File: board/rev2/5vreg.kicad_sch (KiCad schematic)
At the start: 20 parts

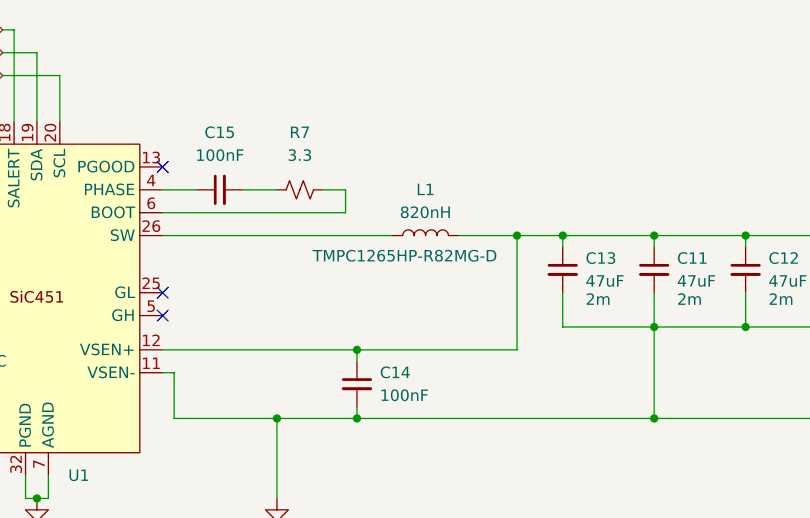
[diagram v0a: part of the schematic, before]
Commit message: Continue board work
- move to rp2040, separate stm32g071 to do usb-c + aux ctrl IO
  - still cheaper lol with the cost of stm32s
- more power reg stuff
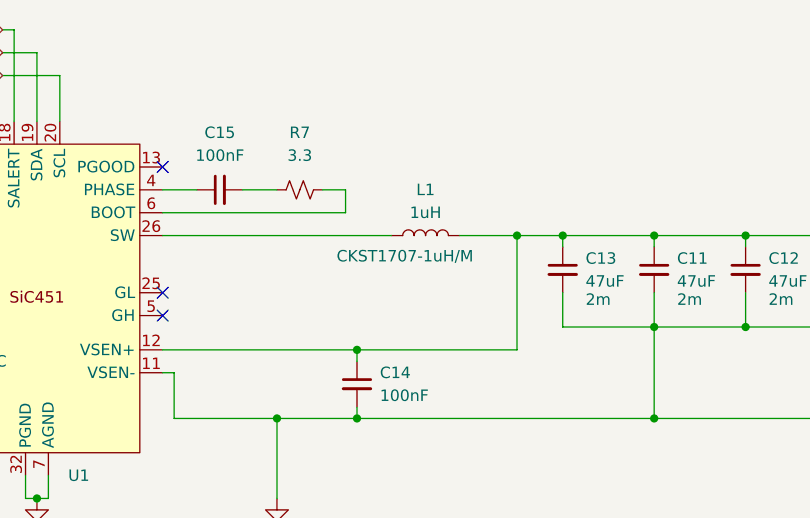
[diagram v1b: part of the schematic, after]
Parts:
- L1: value 820nH -> 1uH; Part TMPC1265HP-R82MG-D -> CKST1707-1uH/M
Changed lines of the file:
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@@
 			)
 		)
-		(property "Value" "820nH"
+		(property "Value" "1uH"
 			(at 198.12 85.09 90)
 			(effects
@@
 			)
 		)
-		(property "Part" "TMPC1265HP-R82MG-D"
+		(property "Part" "CKST1707-1uH/M"
 			(at 195.834 89.916 90)
 			(effects

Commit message: Board GPIO allocation
- and usbmux

still need to do termination on the big buses + a bunch of bypass caps
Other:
- company: (none) -> MLABS
- title: (none) -> USB PD 5V Regulator
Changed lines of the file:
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@@
 	(generator_version "9.0")
 	(paper "A4")
+	(title_block
+		(title "USB PD 5V Regulator")
+		(rev "A")
+		(company "MLABS")
+		(comment 1 "MSign-NG")
+	)
 	(junction
 		(at 68.58 80.01)

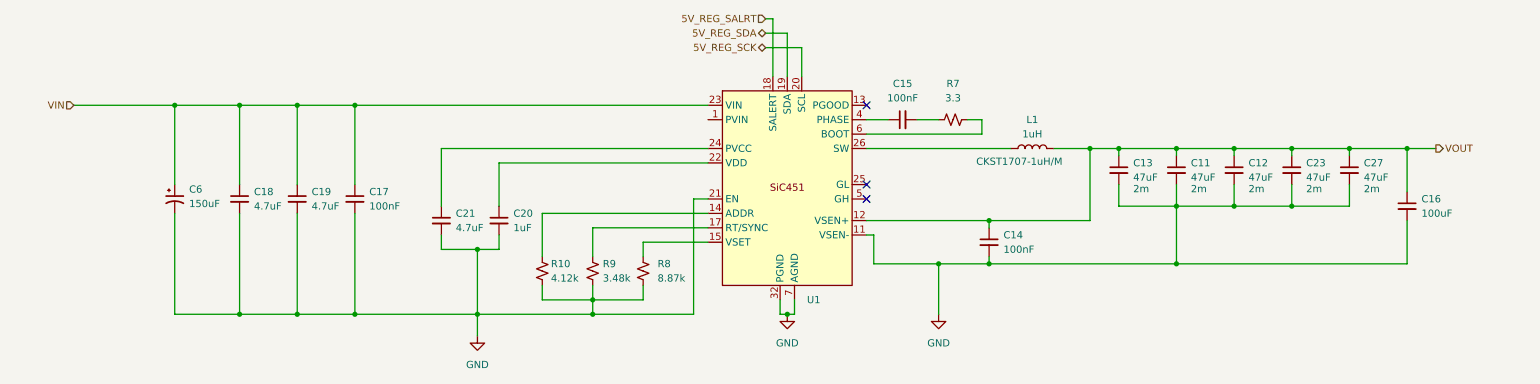
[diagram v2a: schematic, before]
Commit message: Continue board, assign caps/res, adjust for JLC availability
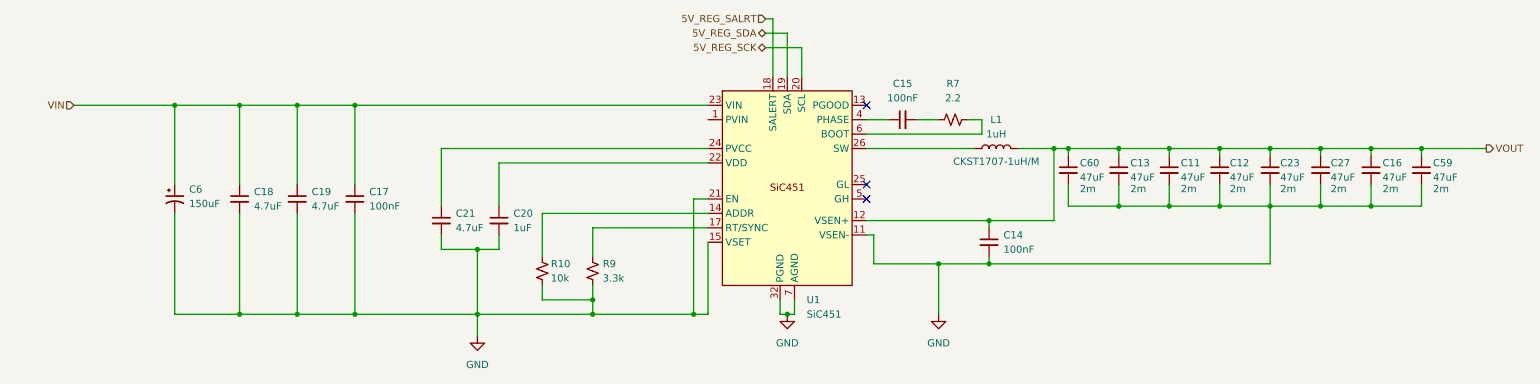
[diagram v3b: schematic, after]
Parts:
- removed R8: 8.87k, symbol Device:R_Small_US
- added C59, C60: 47uF, Capacitor_SMD:C_1206_3216Metric, symbol Device:C_Small
- C11, C12, C13, C23, C27: footprint (none) -> Capacitor_SMD:C_1206_3216Metric; Part (none) -> CL31A476MPHNNNE
- C14, C15, C17: footprint (none) -> Capacitor_SMD:C_0402_1005Metric; Part (none) -> CL05B104KB54PNC
- C16: value 100uF -> 47uF; footprint (none) -> Capacitor_SMD:C_1206_3216Metric; ESR (none) -> 2m; Part (none) -> CL31A476MPHNNNE
- C18, C19, C21: footprint (none) -> Capacitor_SMD:C_1206_3216Metric; Part (none) -> 1206B475K500NT
- C20: footprint (none) -> Capacitor_SMD:C_0603_1608Metric; Part (none) -> CL10A105KB8NNNC
- C6: footprint (none) -> Capacitor_THT:CP_Radial_D8.0mm_P3.50mm; Part (none) -> ERS1VM151F12OT
- L1: footprint (none) -> Inductor_Cenker:L_Cenker_CKST1707
- R10: value 4.12k -> 10k; footprint (none) -> Resistor_SMD:R_0805_2012Metric; Part (none) -> 0805W8F1002T5E
- R7: value 3.3 -> 2.2; footprint (none) -> Resistor_SMD:R_0603_1608Metric; Part (none) -> 0603WAF220KT5E
- R9: value 3.48k -> 3.3k; footprint (none) -> Resistor_SMD:R_0402_1005Metric; Part (none) -> 0402WGF3301TCE
- U1: value ~ -> SiC451
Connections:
- net GND: now also U1.15 (VSET), C59.2, C60.2
- net VOUT: now also C59.1, C60.1
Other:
- moved on the sheet: C11, C12, C23, C27, L1

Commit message: Start new PCB
- all footprints setup
- need to setup netclasses next, tho
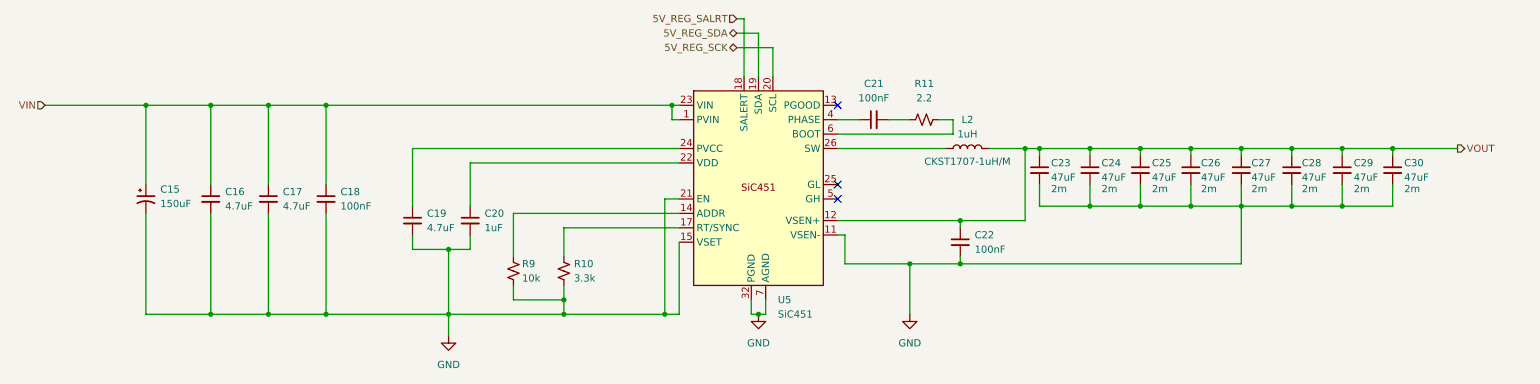
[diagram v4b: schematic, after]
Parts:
- U5: renamed from U1; Part (none) -> SiC451
- renumbered C6 to C15, C18 to C16, C19 to C17, C17 to C18, C21 to C19, C15 to C21, C14 to C22, C60 to C23, C13 to C24, C11 to C25, C12 to C26, C23 to C27, C27 to C28, C16 to C29, C59 to C30, L1 to L2, R9 to R10, R7 to R11, R10 to R9
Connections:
- net VIN: now also U5.1 (PVIN)
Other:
- moved on the sheet: C15, C16, C17, C18, C19, C20, C21, C22, C23, C24, C25, C26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

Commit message: Really finish rev2 board schematic
- fix some more footprints
  - move to real SD card holder, for example
- repair part numbers
- add LCSC part refs to everything
- add even more caps to the 3.3V reg output
  - really should use an LDO but meh it should be fine

total BOM cost for 5 of them is apparently 160 CAD, or like 32 dollars
each (don't think that includes the feeder fees tho)
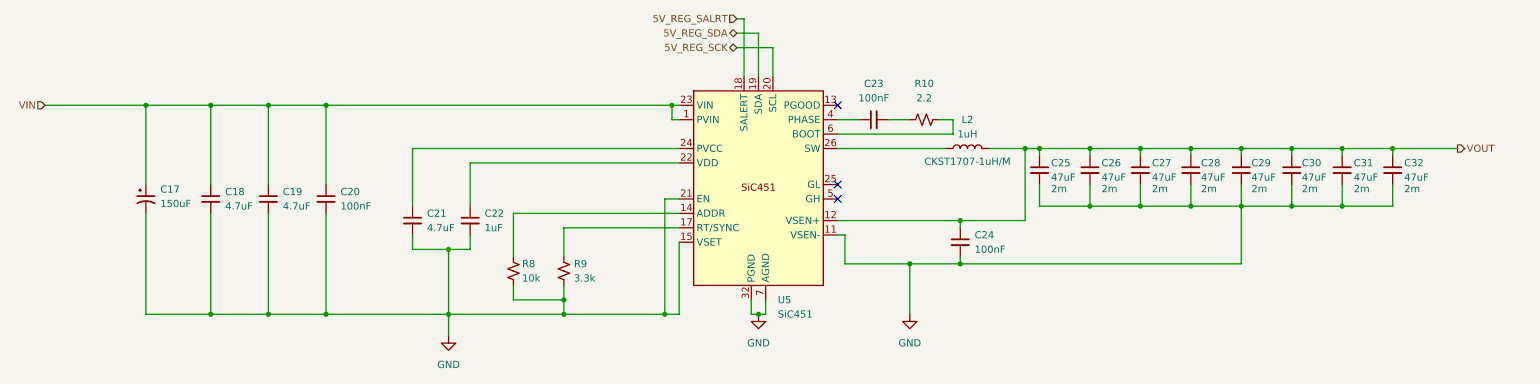
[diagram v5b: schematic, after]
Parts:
- C17: renamed from C15; LCSC (none) -> C106696
- C18: renamed from C16; LCSC (none) -> C29823
- C19: renamed from C17; LCSC (none) -> C29823
- C20: renamed from C18; LCSC (none) -> C307331
- C21: renamed from C19; LCSC (none) -> C29823
- C22: renamed from C20; LCSC (none) -> C15849
- C23: renamed from C21; LCSC (none) -> C307331
- C24: renamed from C22; LCSC (none) -> C307331
- C25: renamed from C23; LCSC (none) -> C96123
- C26: renamed from C24; LCSC (none) -> C96123
- C27: renamed from C25; LCSC (none) -> C96123
- C28: renamed from C26; LCSC (none) -> C96123
- C29: renamed from C27; LCSC (none) -> C96123
- C30: renamed from C28; LCSC (none) -> C96123
- C31: renamed from C29; LCSC (none) -> C96123
- C32: renamed from C30; LCSC (none) -> C96123
- L2: LCSC (none) -> C5292052
- R10: renamed from R11; LCSC (none) -> C22939
- R8: renamed from R9; LCSC (none) -> C17414
- R9: renamed from R10; LCSC (none) -> C25890
- U5: LCSC (none) -> C1852144; Part SiC451 -> SIC451ED-T1-GE3

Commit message: Start board
add a few extra bypass caps too, and swap some pins on the USB mux

i forgot to add a bypass cap on the tpd6s so that also needs to happen

truly 63 capacitors is not enough
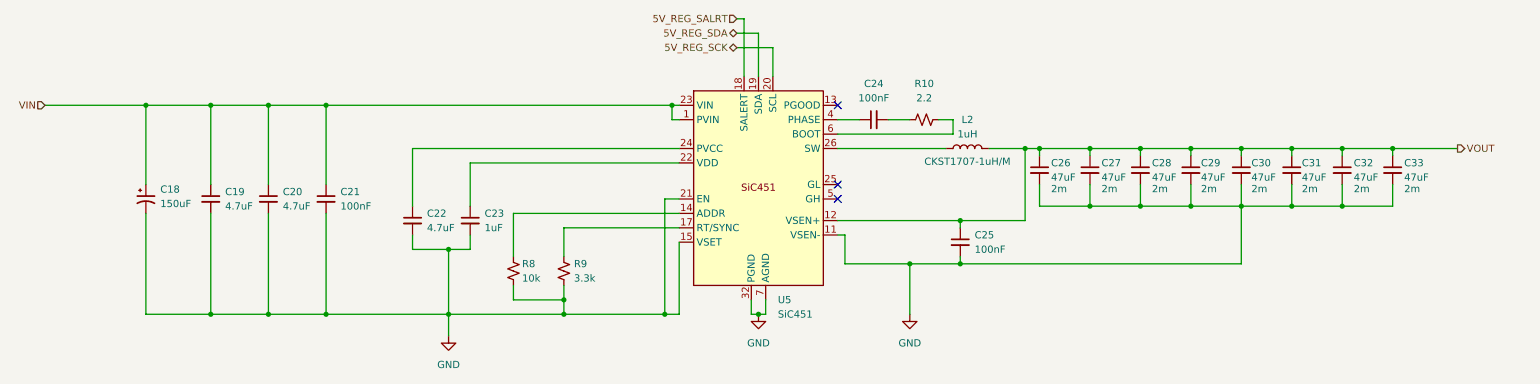
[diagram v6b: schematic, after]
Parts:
- renumbered C17 to C18, C18 to C19, C19 to C20, C20 to C21, C21 to C22, C22 to C23, C23 to C24, C24 to C25, C25 to C26, C26 to C27, C27 to C28, C28 to C29, C29 to C30, C30 to C31, C31 to C32, C32 to C33
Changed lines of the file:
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@@
 		(dnp no)
 		(fields_autoplaced yes)
-		(property "Reference" "C24"
+		(property "Reference" "C25"
 			(at 187.96 102.8762 0)
 			(effects
@@
 			(project ""
 				(path "/32eb05c7-b4a6-42f3-8fb3-43453631100f/802d77e5-f72d-443e-abfe-d20b44acef6c/d8dbf604-5384-4c21-88e4-d3f4969843cb"
-					(reference "C24")
+					(reference "C25")
 					(unit 1)
 				)
@@
 		(dnp no)
 		(fields_autoplaced yes)
-		(property "Reference" "C22"
+		(property "Reference" "C23"
 			(at 101.6 99.0662 0)
 			(effects
@@
 			(project ""
 				(path "/32eb05c7-b4a6-42f3-8fb3-43453631100f/802d77e5-f72d-443e-abfe-d20b44acef6c/d8dbf604-5384-4c21-88e4-d3f4969843cb"
-					(reference "C22")
+					(reference "C23")
 					(unit 1)
 				)
@@
 		(dnp no)
 		(fields_autoplaced yes)
-		(property "Reference" "C19"
+		(property "Reference" "C20"
 			(at 66.04 95.2562 0)
 			(effects
@@
 			(project "mainboard"
 				(path "/32eb05c7-b4a6-42f3-8fb3-43453631100f/802d77e5-f72d-443e-abfe-d20b44acef6c/d8dbf604-5384-4c21-88e4-d3f4969843cb"
-					(reference "C19")
+					(reference "C20")
 					(unit 1)
 				)
@@
 		(on_board yes)
 		(dnp no)
-		(property "Reference" "C32"
+		(property "Reference" "C33"
 			(at 263.652 90.17 0)
 			(effects
@@
 			(project "mainboard"
 				(path "/32eb05c7-b4a6-42f3-8fb3-43453631100f/802d77e5-f72d-443e-abfe-d20b44acef6c/d8dbf604-5384-4c21-88e4-d3f4969843cb"
-					(reference "C32")
+					(reference "C33")
 					(unit 1)
 				)
@@
 		(dnp no)
 		(fields_autoplaced yes)
-		(property "Reference" "C23"
+		(property "Reference" "C24"
 			(at 170.1863 76.2 90)
 			(effects
@@
 			(project ""
 				(path "/32eb05c7-b4a6-42f3-8fb3-43453631100f/802d77e5-f72d-443e-abfe-d20b44acef6c/d8dbf604-5384-4c21-88e4-d3f4969843cb"
-					(reference "C23")
+					(reference "C24")
 					(unit 1)
 				)
@@
 		(on_board yes)
 		(dnp no)
-		(property "Reference" "C25"
+		(property "Reference" "C26"
 			(at 201.422 90.17 0)
 			(effects
@@
 			(project "mainboard"
 				(path "/32eb05c7-b4a6-42f3-8fb3-43453631100f/802d77e5-f72d-443e-abfe-d20b44acef6c/d8dbf604-5384-4c21-88e4-d3f4969843cb"
-					(reference "C25")
+					(reference "C26")
 					(unit 1)
 				)
@@
 		(on_board yes)
 		(dnp no)
-		(property "Reference" "C28"
+		(property "Reference" "C29"
 			(at 227.838 90.17 0)
 			(effects
@@
 			(project "mainboard"
 				(path "/32eb05c7-b4a6-42f3-8fb3-43453631100f/802d77e5-f72d-443e-abfe-d20b44acef6c/d8dbf604-5384-4c21-88e4-d3f4969843cb"
-					(reference "C28")
+					(reference "C29")
 					(unit 1)
 				)
@@
 		(dnp no)
 		(fields_autoplaced yes)
-		(property "Reference" "C20"
+		(property "Reference" "C21"
 			(at 76.2 95.2562 0)
 			(effects
@@
 			(project ""
 				(path "/32eb05c7-b4a6-42f3-8fb3-43453631100f/802d77e5-f72d-443e-abfe-d20b44acef6c/d8dbf604-5384-4c21-88e4-d3f4969843cb"
-					(reference "C20")
+					(reference "C21")
 					(unit 1)
 				)
@@
 		(on_board yes)
 		(dnp no)
-		(property "Reference" "C30"
+		(property "Reference" "C31"
 			(at 245.618 90.17 0)
 			(effects
@@
 			(project "mainboard"
 				(path "/32eb05c7-b4a6-42f3-8fb3-43453631100f/802d77e5-f72d-443e-abfe-d20b44acef6c/d8dbf604-5384-4c21-88e4-d3f4969843cb"
-					(reference "C30")
+					(reference "C31")
 					(unit 1)
 				)
@@
 		(on_board yes)
 		(dnp no)
-		(property "Reference" "C29"
+		(property "Reference" "C30"
 			(at 236.728 90.17 0)
 			(effects
@@
 			(project "mainboard"
 				(path "/32eb05c7-b4a6-42f3-8fb3-43453631100f/802d77e5-f72d-443e-abfe-d20b44acef6c/d8dbf604-5384-4c21-88e4-d3f4969843cb"
-					(reference "C29")
+					(reference "C30")
 					(unit 1)
 				)
@@
 		(dnp no)
 		(fields_autoplaced yes)
-		(property "Reference" "C18"
+		(property "Reference" "C19"
 			(at 55.88 95.2562 0)
 			(effects
@@
 			(project "mainboard"
 				(path "/32eb05c7-b4a6-42f3-8fb3-43453631100f/802d77e5-f72d-443e-abfe-d20b44acef6c/d8dbf604-5384-4c21-88e4-d3f4969843cb"
-					(reference "C18")
+					(reference "C19")
 					(unit 1)
 				)
@@
 		(on_board yes)
 		(dnp no)
-		(property "Reference" "C27"
+		(property "Reference" "C28"
 			(at 219.202 90.17 0)
 			(effects
@@
 			(project "mainboard"
 				(path "/32eb05c7-b4a6-42f3-8fb3-43453631100f/802d77e5-f72d-443e-abfe-d20b44acef6c/d8dbf604-5384-4c21-88e4-d3f4969843cb"
-					(reference "C27")
+					(reference "C28")
 					(unit 1)
 				)
@@
 		(dnp no)
 		(fields_autoplaced yes)
-		(property "Reference" "C17"
+		(property "Reference" "C18"
 			(at 44.45 94.8181 0)
 			(effects
@@
 			(project ""
 				(path "/32eb05c7-b4a6-42f3-8fb3-43453631100f/802d77e5-f72d-443e-abfe-d20b44acef6c/d8dbf604-5384-4c21-88e4-d3f4969843cb"
-					(reference "C17")
+					(reference "C18")
 					(unit 1)
 				)
@@
 		(dnp no)
 		(fields_autoplaced yes)
-		(property "Reference" "C21"
+		(property "Reference" "C22"
 			(at 91.44 99.0662 0)
 			(effects
@@
 			(project ""
 				(path "/32eb05c7-b4a6-42f3-8fb3-43453631100f/802d77e5-f72d-443e-abfe-d20b44acef6c/d8dbf604-5384-4c21-88e4-d3f4969843cb"
-					(reference "C21")
+					(reference "C22")
 					(unit 1)
 				)
@@
 		(on_board yes)
 		(dnp no)
-		(property "Reference" "C26"
+		(property "Reference" "C27"
 			(at 210.312 90.17 0)
 			(effects
@@
 			(project ""
 				(path "/32eb05c7-b4a6-42f3-8fb3-43453631100f/802d77e5-f72d-443e-abfe-d20b44acef6c/d8dbf604-5384-4c21-88e4-d3f4969843cb"
-					(reference "C26")
+					(reference "C27")
 					(unit 1)
 				)
@@
 		(on_board yes)
 		(dnp no)
-		(property "Reference" "C31"
+		(property "Reference" "C32"
 			(at 254.762 90.17 0)
 			(effects
@@
 			(project "mainboard"
 				(path "/32eb05c7-b4a6-42f3-8fb3-43453631100f/802d77e5-f72d-443e-abfe-d20b44acef6c/d8dbf604-5384-4c21-88e4-d3f4969843cb"
-					(reference "C31")
-					(unit 1)
-				)
+					(reference "C32")
+					(unit 1)
+				)

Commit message: More tweaks to schematic, start laying out regulators
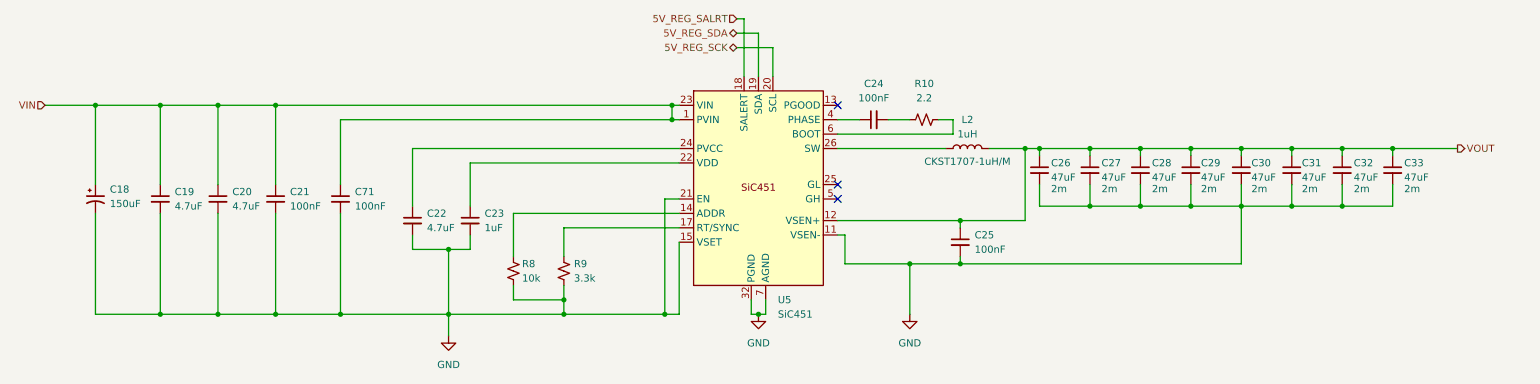
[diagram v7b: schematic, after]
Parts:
- added C71: 100nF, Capacitor_SMD:C_0402_1005Metric, symbol Device:C_Small
- R8: footprint Resistor_SMD:R_0805_2012Metric -> Resistor_SMD:R_0402_1005Metric; LCSC C17414 -> C25744; Part 0805W8F1002T5E -> 0402WGF1002TCE
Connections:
- net GND: now also C71.2
- net VIN: now also C71.1
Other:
- moved on the sheet: C18, C19, C20, C21

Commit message: Finish board rev2
woo another pcb
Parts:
- added NT1, NT2: NetTie_2, NetTie:NetTie-2_SMD_Pad0.5mm, symbol Device:NetTie_2
- added TP7: TestPoint, TestPoint:TestPoint_Pad_D1.0mm, symbol Connector:TestPoint
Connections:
- net GND: now also NT2.2, TP7.1; no longer U5.11 (VSEN-)
- net VOUT: now also NT1.2; no longer U5.12 (VSEN+)
- new net VSEN+: NT1.1, U5.12 (VSEN+)
- new net VSEN-: NT2.1, U5.11 (VSEN-)
